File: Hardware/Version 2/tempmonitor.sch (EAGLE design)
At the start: 31 parts, among them IC1 74LS595D, IC2 74LS595D, IC3 74LS595D, IC4 74LS595D, IC5 74LS595D, Q1 BC848SMD, Q2 BC848SMD, Q3 BC848SMD, U1 TINY85-20-DIP

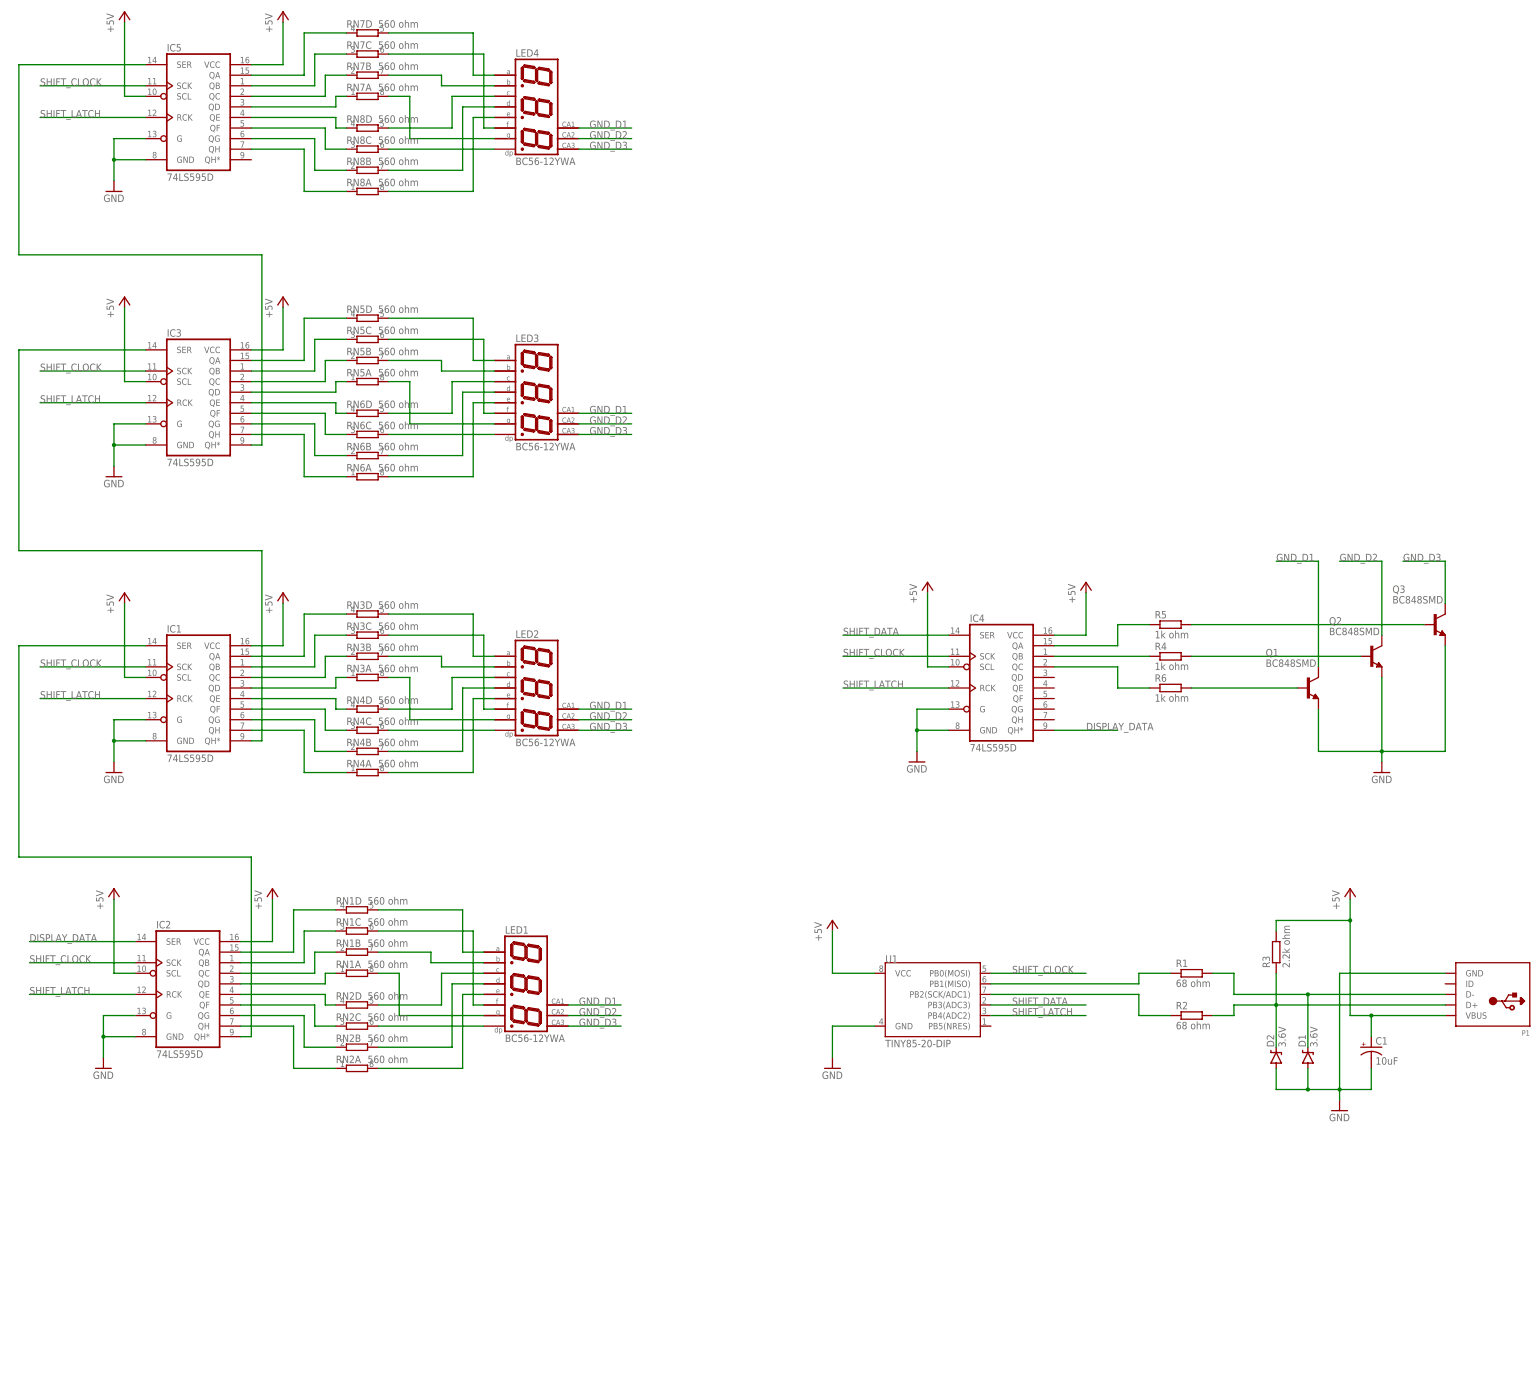
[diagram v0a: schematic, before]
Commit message: PCB layout
PCB routed, need of silkscreen fixes. Directory clean up.
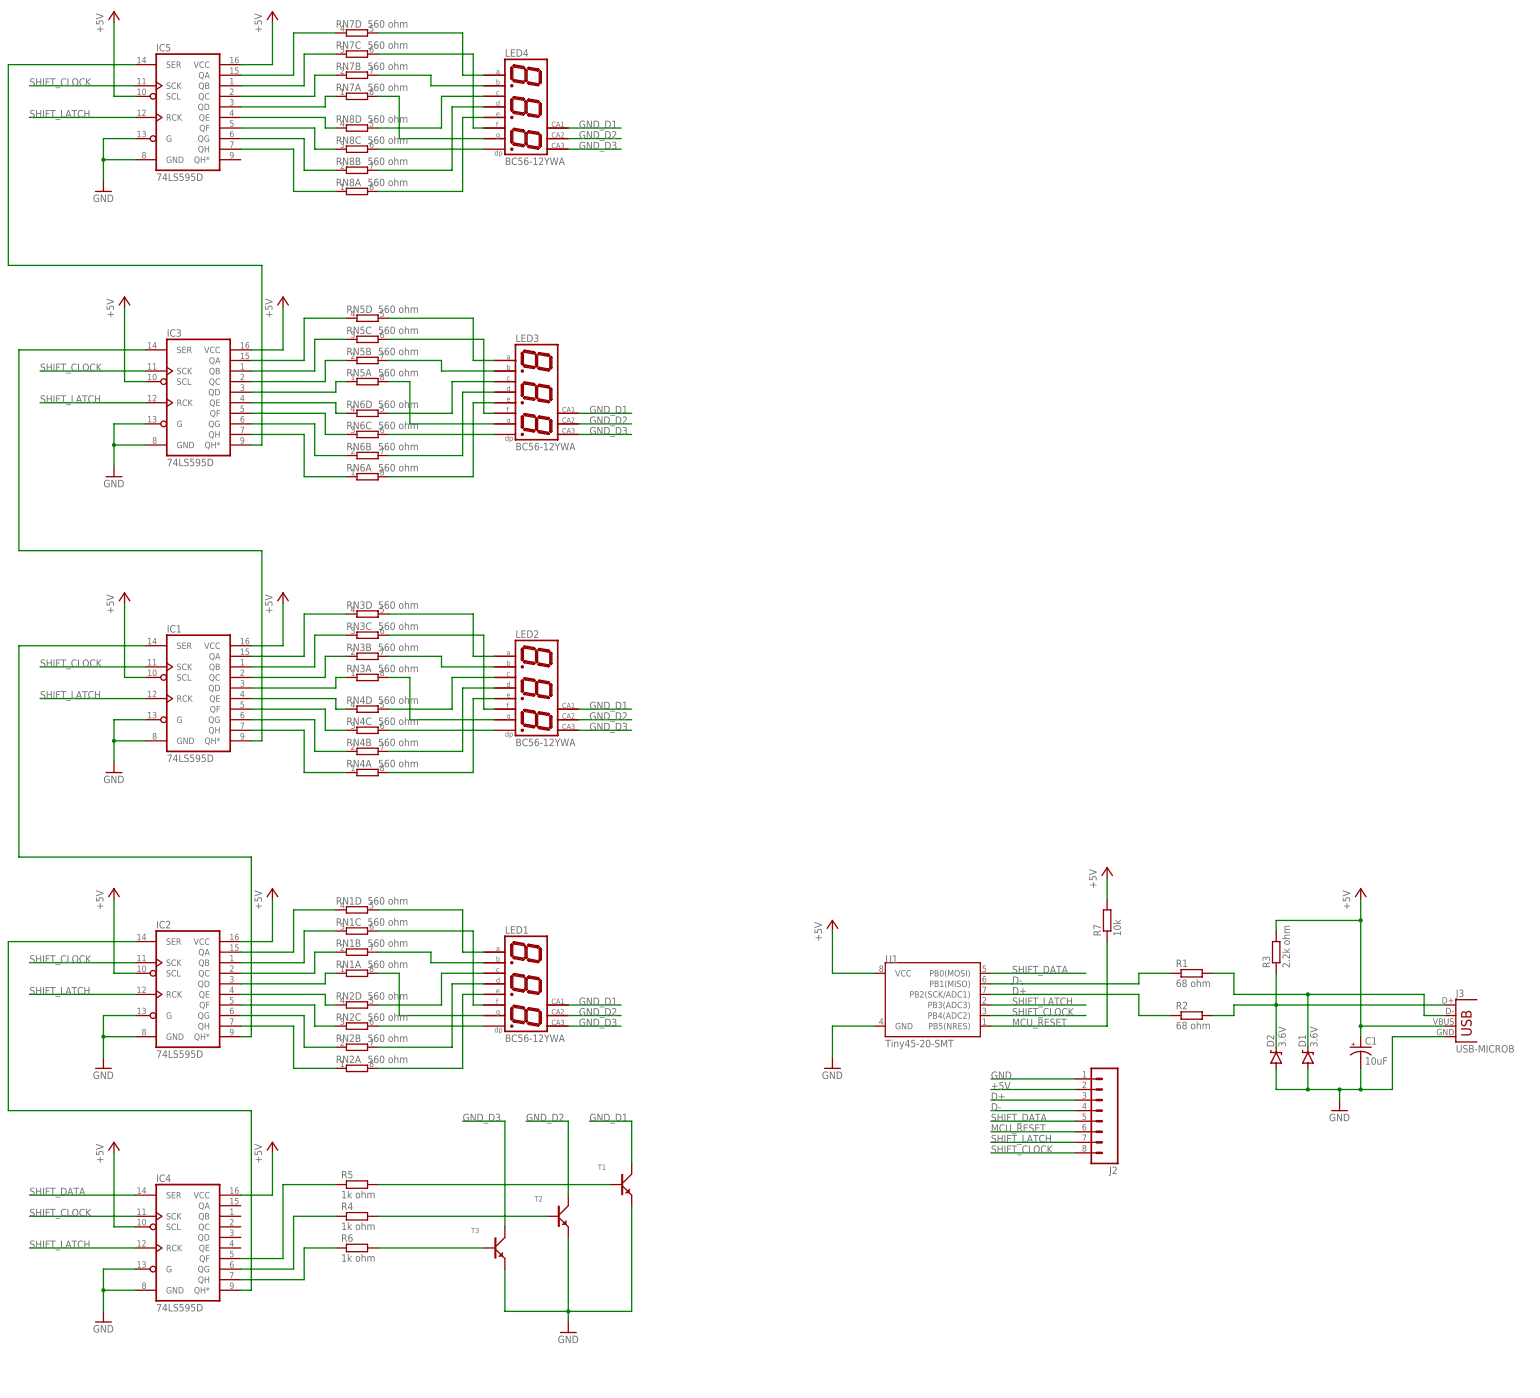
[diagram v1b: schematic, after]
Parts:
- removed P1: (no value), adafruit:USBMINIB
- removed Q1, Q2, Q3: BC848SMD, transistor-npn:BC848SMD
- added J2: TP_8, TempMonitor:TP_8
- added J3: USB-MICROB, SparkFun-Connectors:USB-MICROB
- added R7: 10k, resistor:R-EU_R0805W
- added T1, T2, T3: NPN, TempMonitor:NPN
- C1: device SparkFun-Passives:CAP_POLD -> SparkFun-Capacitors:CAP_POLF80
- U1: value TINY85-20-DIP -> Tiny45-20-SMT; device SparkFun-DigitalIC:ATTINY45TINY85-20-DIP -> SparkFun-DigitalIC:ATTINY45TINY45-20-SMT
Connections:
- net DISPLAY_DATA renamed N$6
- removed net N$34 (its old number): IC4.QC, R6.1
- removed net N$6 (its old number): R1.1, U1.PB1(MISO)
- new net D+: J2.3, R2.1, U1.PB2(SCK/ADC1)
- new net D-: J2.4, R1.1, U1.PB1(MISO)
- new net MCU_RESET: J2.6, R7.1, U1.PB5(NRES)
- net +5V: now also J2.2, J3.VBUS, R7.2; no longer P1.VBUS
- net GND: now also J2.1, J3.GND, T1.E, T2.E, T3.E; no longer P1.GND, Q1.E, Q2.E, Q3.E
- net GND_D1: now also T1.C; no longer Q1.C
- net GND_D2: now also T2.C; no longer Q2.C
- net GND_D3: now also T3.C; no longer Q3.C
- net N$1: now also J3.D-; no longer P1.D-
- net N$2: now also J3.D+; no longer P1.D+
- net N$32: now also IC4.QG; no longer IC4.QB
- net N$33: now also IC4.QF; no longer IC4.QA
- net N$35: now also T2.B; no longer Q2.B
- net N$36: now also T1.B; no longer Q3.B
- net N$37: now also T3.B; no longer Q1.B
- net N$5: now also IC4.QH, R6.1; no longer R2.1, U1.PB2(SCK/ADC1)
- net SHIFT_CLOCK: now also J2.8, U1.PB4(ADC2); no longer U1.PB0(MOSI)
- net SHIFT_DATA: now also J2.5, U1.PB0(MOSI); no longer U1.PB3(ADC3)
- net SHIFT_LATCH: now also J2.7, U1.PB3(ADC3); no longer U1.PB4(ADC2)
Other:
- moved on the sheet: C1, IC4, IC5, LED4, R4, R5, R6, RN7A, RN7B, RN7C, RN7D, RN8A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

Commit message: Added loggos
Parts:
- added LOGO1: OSHW-LOGOL, SparkFun-Aesthetics:OSHW-LOGOL
- added U$1, U$2: LOGO, TempMonitor:LOGO
- added U$3: ROHS_LOGO, SparkFun-Aesthetics:ROHS_LOGO
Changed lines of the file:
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@@
 <grid distance="0.1" unitdist="inch" unit="inch" style="lines" multiple="1" display="no" altdistance="0.01" altunitdist="inch" altunit="inch"/>
 <layers>
-<layer number="1" name="Top" color="4" fill="1" visible="yes" active="no"/>
-<layer number="16" name="Bottom" color="1" fill="1" visible="yes" active="no"/>
-<layer number="17" name="Pads" color="2" fill="1" visible="yes" active="no"/>
-<layer number="18" name="Vias" color="2" fill="1" visible="yes" active="no"/>
-<layer number="19" name="Unrouted" color="6" fill="1" visible="yes" active="no"/>
-<layer number="20" name="Dimension" color="15" fill="1" visible="yes" active="no"/>
-<layer number="21" name="tPlace" color="7" fill="1" visible="yes" active="no"/>
-<layer number="22" name="bPlace" color="7" fill="1" visible="yes" active="no"/>
-<layer number="23" name="tOrigins" color="15" fill="1" visible="yes" active="no"/>
-<layer number="24" name="bOrigins" color="15" fill="1" visible="yes" active="no"/>
-<layer number="25" name="tNames" color="7" fill="1" visible="yes" active="no"/>
-<layer number="26" name="bNames" color="7" fill="1" visible="yes" active="no"/>
-<layer number="27" name="tValues" color="7" fill="1" visible="yes" active="no"/>
-<layer number="28" name="bValues" color="7" fill="1" visible="yes" active="no"/>
+<layer number="1" name="Top" color="4" fill="1" visible="no" active="no"/>
+<layer number="16" name="Bottom" color="1" fill="1" visible="no" active="no"/>
+<layer number="17" name="Pads" color="2" fill="1" visible="no" active="no"/>
+<layer number="18" name="Vias" color="2" fill="1" visible="no" active="no"/>
+<layer number="19" name="Unrouted" color="6" fill="1" visible="no" active="no"/>
+<layer number="20" name="Dimension" color="15" fill="1" visible="no" active="no"/>
+<layer number="21" name="tPlace" color="7" fill="1" visible="no" active="no"/>
+<layer number="22" name="bPlace" color="7" fill="1" visible="no" active="no"/>
+<layer number="23" name="tOrigins" color="15" fill="1" visible="no" active="no"/>
+<layer number="24" name="bOrigins" color="15" fill="1" visible="no" active="no"/>
+<layer number="25" name="tNames" color="7" fill="1" visible="no" active="no"/>
+<layer number="26" name="bNames" color="7" fill="1" visible="no" active="no"/>
+<layer number="27" name="tValues" color="7" fill="1" visible="no" active="no"/>
+<layer number="28" name="bValues" color="7" fill="1" visible="no" active="no"/>
 <layer number="29" name="tStop" color="7" fill="3" visible="no" active="no"/>
 <layer number="30" name="bStop" color="7" fill="6" visible="no" active="no"/>
@@
 <layer number="35" name="tGlue" color="7" fill="4" visible="no" active="no"/>
 <layer number="36" name="bGlue" color="7" fill="5" visible="no" active="no"/>
-<layer number="37" name="tTest" color="7" fill="1" visible="yes" active="no"/>
-<layer number="38" name="bTest" color="7" fill="1" visible="yes" active="no"/>
+<layer number="37" name="tTest" color="7" fill="1" visible="no" active="no"/>
+<layer number="38" name="bTest" color="7" fill="1" visible="no" active="no"/>
 <layer number="39" name="tKeepout" color="4" fill="11" visible="no" active="no"/>
 <layer number="40" name="bKeepout" color="1" fill="11" visible="no" active="no"/>
@@
 <layer number="44" name="Drills" color="7" fill="1" visible="no" active="no"/>
 <layer number="45" name="Holes" color="7" fill="1" visible="no" active="no"/>
-<layer number="46" name="Milling" color="3" fill="1" visible="yes" active="no"/>
-<layer number="47" name="Measures" color="7" fill="1" visible="yes" active="no"/>
-<layer number="48" name="Document" color="7" fill="1" visible="yes" active="no"/>
-<layer number="49" name="Reference" color="7" fill="1" visible="yes" active="no"/>
-<layer number="50" name="dxf" color="7" fill="1" visible="yes" active="no"/>
-<layer number="51" name="tDocu" color="7" fill="1" visible="yes" active="no"/>
-<layer number="52" name="bDocu" color="7" fill="1" visible="yes" active="no"/>
-<layer number="53" name="tGND_GNDA" color="7" fill="9" visible="yes" active="no"/>
-<layer number="54" name="bGND_GNDA" color="1" fill="9" visible="yes" active="no"/>
-<layer number="56" name="wert" color="7" fill="1" visible="yes" active="no"/>
-<layer number="57" name="tCAD" color="7" fill="1" visible="yes" active="no"/>
-<layer number="59" name="tCarbon" color="7" fill="1" visible="yes" active="no"/>
-<layer number="60" name="bCarbon" color="7" fill="1" visible="yes" active="no"/>
+<layer number="46" name="Milling" color="3" fill="1" visible="no" active="no"/>
+<layer number="47" name="Measures" color="7" fill="1" visible="no" active="no"/>
+<layer number="48" name="Document" color="7" fill="1" visible="no" active="no"/>
+<layer number="49" name="Reference" color="7" fill="1" visible="no" active="no"/>
+<layer number="50" name="dxf" color="7" fill="1" visible="no" active="no"/>
+<layer number="51" name="tDocu" color="7" fill="1" visible="no" active="no"/>
+<layer number="52" name="bDocu" color="7" fill="1" visible="no" active="no"/>
+<layer number="53" name="tGND_GNDA" color="7" fill="9" visible="no" active="no"/>
+<layer number="54" name="bGND_GNDA" color="1" fill="9" visible="no" active="no"/>
+<layer number="56" name="wert" color="7" fill="1" visible="no" active="no"/>
+<layer number="57" name="tCAD" color="7" fill="1" visible="no" active="no"/>
+<layer number="59" name="tCarbon" color="7" fill="1" visible="no" active="no"/>
+<layer number="60" name="bCarbon" color="7" fill="1" visible="no" active="no"/>
 <layer number="90" name="Modules" color="5" fill="1" visible="yes" active="yes"/>
 <layer number="91" name="Nets" color="2" fill="1" visible="yes" active="yes"/>
@@
 <part name="P+13" library="supply1" deviceset="+5V" device=""/>
 <part name="J3" library="SparkFun-Connectors" deviceset="USB" device="-MICROB"/>
+<part name="U$1" library="TempMonitor" deviceset="LOGO" device=""/>
+<part name="U$2" library="TempMonitor" deviceset="LOGO" device=""/>
+<part name="LOGO1" library="SparkFun-Aesthetics" deviceset="OSHW-LOGO" device="L"/>
+<part name="U$3" library="SparkFun-Aesthetics" deviceset="ROHS_LOGO" device=""/>
 </parts>
 <sheets>
@@
 <instance part="P+13" gate="1" x="259.08" y="198.12"/>
 <instance part="J3" gate="G$1" x="342.9" y="157.48"/>
+<instance part="U$1" gate="G$1" x="210.82" y="96.52"/>
+<instance part="U$2" gate="G$1" x="180.34" y="96.52"/>
+<instance part="LOGO1" gate="G$1" x="248.92" y="101.6"/>
+<instance part="U$3" gate="G$1" x="264.16" y="91.44"/>
 </instances>
 <busses>

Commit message: USB circuit fix
USB circuit fix R3 incorrectly connected. Added filtering capacitors to MCU and shift registers. Centered displays.
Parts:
- removed U$3: ROHS_LOGO, SparkFun-Aesthetics:ROHS_LOGO
- added C2, C3, C4, C5, C6: 0.1uF, resistor:C-EUC0805
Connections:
- net +5V: now also C2.1, C3.1, C4.1, C5.1, C6.2
- net GND: now also C2.2, C3.2, C4.2, C5.2, C6.1
- net N$1: now also R3.1
- net N$2: no longer R3.1
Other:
- moved on the sheet: IC5, LED4, R3, RN7A, RN7B, RN7C, RN7D, RN8A, RN8B, RN8C, RN8D
